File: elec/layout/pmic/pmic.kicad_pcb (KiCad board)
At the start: 2 copper layers, 14 parts, among them U1 _PCA9450AAHNY

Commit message: Fixing build errors
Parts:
- added C10, C9: 4.7µF ±10% 16V X5R, lcsc:C0603, F.Cu at (0.00, 0.00)
- added C11, C12, C13, C14, C8: 1µF ±20% 6.3V X5R, lcsc:C0201, F.Cu at (0.00, 0.00)
- added C15: 82nF ±5% 25V X7R, lcsc:C0603, F.Cu at (0.00, 0.00)
- added R1: 10kΩ ±1% 62.5mW, lcsc:R0402, F.Cu at (0.00, 0.00)
- added R2: 750mΩ ±5% 100mW, lcsc:R0603, F.Cu at (0.00, 0.00)
- C7: value 82nF ±5% 25V X7R -> 1µF ±20% 6.3V X5R; footprint lcsc:C0603 -> lcsc:C0201
- L1, L2, L3, L5, L6: value 470nH ±30% 3A - infA -> 470nH ±20% 3A - infA
- L4: value 1µH ±30% 3A - infA -> 1µH ±20% 3A - infA
- moved L1 22.6 mm to (165.1, 82.8), turned to -90 degrees
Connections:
- net *3A58.pmic-hv-0 renamed NVCC_DRAM_1V1
- net *3A58.pmic-hv-1 renamed VDD_1V8
- net *3A58.pmic-hv-2 renamed VDD_DRAM_0V9
- net *3A58.pmic-hv-3 renamed VDD_ARM_0V9
- net *3A58.pmic-hv-4 renamed VDD_SOC_0V8
- net *3A58.pmic-net-2 renamed VDD_1V8_SW
- net *3A58.pmic-net-3 renamed VDD_DRAM_0V9_SW
- net *3A58.pmic-net-4 renamed VDD_ARM_0V9_SW
- net *3A58.pmic-net-5 renamed VDD_SOC_0V8_SW
- net hv renamed VCC_3V3
- C1 pad 2: lv -> GND
- C2 pad 2: lv -> GND
- C3 pad 2: lv -> GND
- C4 pad 2: lv -> GND
- C5 pad 2: lv -> GND
- C6 pad 2: lv -> GND
- C7 pad 1: *3A58.pmic-net-6 -> NVCC_SD2
- C7 pad 2: lv -> *3A58.pmic.NVCC_SD2-lv
- L5 pad 1: *3A58.pmic-net-1 -> VDD_PHY_0V9_SW
- L6 pad 1: *3A58.pmic-net-0 -> VDDA_1V8_SW
- U1 pad 1: ldo4 -> VDD_PHY_0V9
- U1 pad 15: *3A58.pmic-net-1 -> VDD_PHY_0V9_SW
- U1 pad 16: *3A58.pmic-net-6 -> VSYS_5V
- U1 pad 17: *3A58.pmic-net-6 -> VSYS_5V
- U1 pad 18: *3A58.pmic-net-6 -> VSYS_5V
- U1 pad 2: ldo2 -> VDD_SNVS_0V8
- U1 pad 23: swout -> *3A58.pmic-net-0
- U1 pad 3: ldo1 -> NVCC_SNVS_1V8
- U1 pad 33: *3A58.pmic-net-6 -> VSYS_5V
- U1 pad 34: *3A58.pmic-net-6 -> VSYS_5V
- U1 pad 35: *3A58.pmic-net-6 -> VSYS_5V
- U1 pad 43: lv -> GND
- U1 pad 47: *3A58.pmic-net-6 -> VSYS_5V
- U1 pad 5: lv -> GND
- U1 pad 50: *3A58.pmic-net-0 -> VDDA_1V8_SW
- U1 pad 51: *3A58.pmic-net-0 -> VDDA_1V8_SW
- U1 pad 54: ldo3 -> VDDA_1V8
- U1 pad 55: ldo5 -> NVCC_SD2
- U1 pad 56: *3A58.pmic-net-6 -> VSYS_5V
- U1 pad 57: lv -> GND
- U1 pad 6: rtc_reset_b -> *3A58.pmic-net-1

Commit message: pmic layout file
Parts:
- added C16: 2.2µF ±20% 10V X5R, lcsc:C0402, B.Cu at (168.4, 88.9)
- added C17: 2.2µF ±20% 10V X5R, lcsc:C0402, B.Cu at (162.9, 88.7)
- added C18: 10µF ±10% 10V X5R, lcsc:C0603, B.Cu at (163.0, 91.2)
- added C19: 10µF ±10% 10V X5R, lcsc:C0603, B.Cu at (163.0, 90.2)
- added C20: 10µF ±10% 10V X5R, lcsc:C0603, B.Cu at (166.9, 86.3)
- added C21: 10µF ±10% 10V X5R, lcsc:C0603, B.Cu at (167.9, 86.3)
- added C22: 10µF ±10% 10V X5R, lcsc:C0603, B.Cu at (168.2, 90.8)
- added C23: 10µF ±10% 10V X5R, lcsc:C0603, B.Cu at (168.2, 89.8)
- added C24: 10µF ±10% 10V X5R, lcsc:C0603, B.Cu at (163.0, 87.9)
- added C25: 2.2µF ±20% 10V X5R, lcsc:C0402, B.Cu at (165.0, 86.4)
- added C26: 10pF ±5% 50V C0G, lcsc:C0201, F.Cu at (167.5, 93.7)
- added C27: 10pF ±5% 50V C0G, lcsc:C0201, F.Cu at (166.3, 93.7)
- added XTAL1: Crystal, lcsc:OSC-SMD_L3.2-W1.5, F.Cu at (166.9, 94.8)
- C1, C11, C12, C13, C14, C2, C3, C4, C5, C6, C7, C8, C9: moved to B.Cu
- C15: value 82nF ±5% 25V X7R -> 10µF ±10% 10V X5R; moved to B.Cu
- R1: value 10kΩ ±1% 62.5mW -> 10kΩ ±1% 50mW; footprint lcsc:R0402 -> lcsc:R0201; moved to B.Cu
- R2: value 750mΩ ±5% 100mW -> 1.5Ω ±5% 50mW; footprint lcsc:R0603 -> lcsc:R0201; moved to B.Cu
- moved C10 192.6 mm to (171.4, 87.7)
- moved R2 189.4 mm to (161.4, 99.2), turned to -90 degrees
- moved C13 189.1 mm to (161.0, 99.2), turned to -90 degrees
- moved C9 188.4 mm to (160.2, 99.2), turned to -90 degrees
- moved C14 187.6 mm to (159.2, 99.2), turned to -90 degrees
- moved R1 187.1 mm to (158.6, 99.2), turned to -90 degrees
- moved C15 187.0 mm to (165.9, 86.3), turned to -90 degrees
- moved C8 186.7 mm to (158.2, 99.2), turned to -90 degrees
- moved C12 186.4 mm to (157.8, 99.2), turned to -90 degrees
- moved C11 184.8 mm to (161.0, 90.7), turned to 180 degrees
- moved C4 33.5 mm to (172.1, 88.9), turned to 180 degrees
- moved C5 33.2 mm to (171.7, 91.3), turned to 180 degrees
- moved C3 30.1 mm to (167.5, 83.1), turned to -90 degrees
- moved L5 29.1 mm to (171.7, 91.8), turned to 180 degrees
- moved L3 27.2 mm to (167.5, 83.1), turned to -90 degrees
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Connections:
- net *3A58.pmic-lv renamed *3B78.pmic-lv
- net *3A58.pmic-net-1 renamed *3B78.pmic-net-3
- net *3A58.pmic.VDD_PHY_1V2-lv renamed *3B78.pmic.VDD_PHY_1V2-lv
- net *3A58.pmic.pmic-net renamed *3B78.pmic.pmic-net
- net signal renamed RTC_RESET_B
- C10 pad 1: *3A58.pmic-net-0 -> VCC_3V3
- C11 pad 2: *3A58.pmic.VDDA_1V8-lv -> GND
- C12 pad 2: *3A58.pmic.VDD_PHY_0V9-lv -> GND
- C14 pad 2: *3A58.pmic.VDD_SNVS_0V8-lv -> GND
- C7 pad 2: *3A58.pmic.NVCC_SD2-lv -> GND
- C8 pad 2: *3A58.pmic.NVCC_SNVS_1V8-lv -> GND
- R2 pad 2: *3A58.pmic-net-0 -> *3B78.pmic-net-2
- U1 pad 10: xtal_in -> *3B78.pmic-net-1
- U1 pad 11: xtal_out -> *3B78.pmic-net-0
- U1 pad 12: sw_en -> *3B78.pmic-net-2
- U1 pad 23: *3A58.pmic-net-0 -> VCC_3V3
- U1 pad 43: GND -> buck_agnd
- U1 pad 5: GND -> agnd
- U1 pad 57: GND -> ep
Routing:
- net *3B78.pmic-net-0: track 0.00 -> 2.88 mm
- net *3B78.pmic-net-1: track 0.00 -> 2.83 mm

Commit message: Layout 90% complete
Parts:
- added C28: 10pF ±5% 50V C0G, lcsc:C0201, F.Cu at (165.7, 93.6)
- C15: value 10µF ±10% 10V X5R -> 1µF ±20% 6.3V X5R; footprint lcsc:C0603 -> lcsc:C0201
- C16, C25: value 2.2µF ±20% 10V X5R -> 10µF ±10% 10V X5R; footprint lcsc:C0402 -> lcsc:C0603
- C18: value 10µF ±10% 10V X5R -> 2.2µF ±20% 10V X5R; footprint lcsc:C0603 -> lcsc:C0402
- C26: value 10pF ±5% 50V C0G -> 2.2µF ±20% 10V X5R; footprint lcsc:C0201 -> lcsc:C0402; moved to B.Cu
- R1: moved to F.Cu
- moved C9 15.1 mm to (172.2, 90.0), turned to 180 degrees
- moved R2 8.99 mm to (167.4, 92.5), turned to 90 degrees
- moved C8 8.85 mm to (163.8, 92.4), turned to 90 degrees
- moved C12 8.55 mm to (162.9, 92.4), turned to 90 degrees
- moved R1 8.08 mm to (164.7, 93.9)
- moved C14 8.02 mm to (163.4, 92.4), turned to 90 degrees
- moved C26 7.50 mm to (166.0, 86.3), turned to -90 degrees
- moved C15 6.22 mm to (164.3, 92.4), turned to 90 degrees
- moved C13 4.74 mm to (163.2, 95.0)
- moved C25 2.01 mm to (163.1, 86.9), turned to 0 degrees
- moved C27 1.18 mm to (167.4, 93.6), turned to 180 degrees
- moved C16 0.25 mm to (168.2, 88.7)
- moved C18 0.11 mm to (163.0, 91.1)
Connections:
- net *3B78.pmic-net-2 renamed *3AE8.pmic-net-0
- net *3B78.pmic-net-3 renamed *3AE8.pmic-net-2
- net *3B78.pmic.VDD_PHY_1V2-lv renamed lv
- net *3B78.pmic.pmic-net renamed *3AE8.pmic.pmic-net
- net VDD_1V8_SW renamed VDD_3V3_SW
- C10 pad 2: *3B78.pmic-lv -> GND
- C15 pad 1: VSYS_5V -> *3AE8.pmic-net-4
- C26 pad 1: *3B78.pmic-net-0 -> VSYS_5V
- C27 pad 1: *3B78.pmic-net-1 -> *3AE8.pmic-net-1
- U1 pad 10: *3B78.pmic-net-1 -> *3AE8.pmic-net-3
- U1 pad 11: *3B78.pmic-net-0 -> *3AE8.pmic-net-1
- U1 pad 14: buck5fb -> VDD_1V8
- U1 pad 21: VDD_1V8 -> VCC_3V3
- U1 pad 4: vint -> *3AE8.pmic-net-4
- U1 pad 43: buck_agnd -> GND
- U1 pad 5: agnd -> GND
- U1 pad 53: vsys -> VSYS_5V
- U1 pad 57: ep -> GND
- XTAL1 pad 1: *3B78.pmic-net-0 -> *3AE8.pmic-net-1
- XTAL1 pad 2: *3B78.pmic-net-1 -> *3AE8.pmic-net-3
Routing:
- net GND: track 0.00 -> 8.49 mm, vias 0 -> 20
- net *3B78.pmic-net-0: track 2.88 -> 0.00 mm
- net *3AE8.pmic-net-0: track 0.00 -> 2.88 mm
- net *3B78.pmic-net-1: track 2.83 -> 0.00 mm
- net *3AE8.pmic-net-2: track 0.00 -> 2.83 mm
- net *3AE8.pmic-net-4: track 0.00 -> 1.37 mm
- net VCC_3V3: track 0.00 -> 1.30 mm, vias 0 -> 3
- net NVCC_SNVS_1V8: track 0.00 -> 1.10 mm, vias 0 -> 1
- net VDD_SNVS_0V8: track 0.00 -> 1.10 mm, vias 0 -> 1
- net *3AE8.pmic-net-1: track 0.00 -> 1.10 mm, vias 0 -> 1
- net *3AE8.pmic-net-3: track 0.00 -> 1.08 mm, vias 0 -> 1
- net VDD_PHY_0V9: track 0.00 -> 1.07 mm, vias 0 -> 1
- net VDDA_1V8: track 0.00 -> 0.86 mm, vias 0 -> 1
- net NVCC_SD2: track 0.00 -> 0.85 mm, vias 0 -> 1
- net VDD_1V8: track 0.00 -> 0.45 mm, vias 0 -> 1
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- added copper zone on F.Cu, net VCC_3V3
- added copper zone on F.Cu, net VDDA_1V8_SW
- added copper zone on F.Cu, net VDD_3V3_SW
- added copper zone on F.Cu, net VDD_ARM_0V9_SW
- added copper zone on F.Cu, net VDD_PHY_0V9_SW
- added copper zone on F.Cu, net VDD_SOC_0V8_SW
- added copper zone on F.Cu, net VSYS_5V

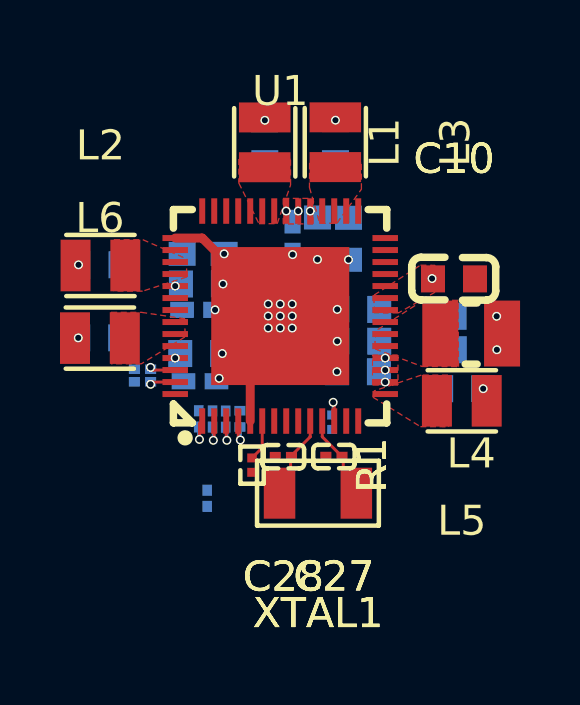
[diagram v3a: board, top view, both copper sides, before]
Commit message: add extra LDO for 1v2 rail
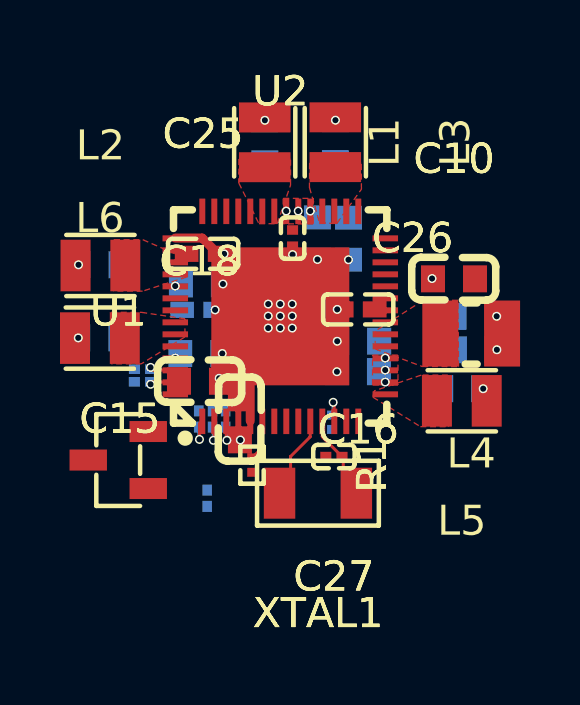
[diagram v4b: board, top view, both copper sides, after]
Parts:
- removed C28: 10pF ±5% 50V C0G, lcsc:C0201
- added U2: _PCA9450AAHNY, lcsc:HVQFN-56_L7.0-W7.0-P0.40-BL-EP4.6, F.Cu at (165.6, 88.9)
- C15: value 1µF ±20% 6.3V X5R -> 10µF ±10% 10V X5R; footprint lcsc:C0201 -> lcsc:C0603; moved to F.Cu
- C16, C25: value 10µF ±10% 10V X5R -> 2.2µF ±20% 10V X5R; footprint lcsc:C0603 -> lcsc:C0402; moved to F.Cu
- C18: value 2.2µF ±20% 10V X5R -> 10µF ±10% 10V X5R; footprint lcsc:C0402 -> lcsc:C0603; moved to F.Cu
- C26: value 2.2µF ±20% 10V X5R -> 10pF ±5% 50V C0G; footprint lcsc:C0402 -> lcsc:C0201; moved to F.Cu
- U1: value _PCA9450AAHNY -> LDO 1.2V Vin max 3.3V - infV Iq; footprint lcsc:HVQFN-56_L7.0-W7.0-P0.40-BL-EP4.6 -> lcsc:SOT-23-3_L2.9-W1.3-P1.90-LS2.4-BR
- moved U1 7.22 mm to (160.2, 93.7)
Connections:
- C13 pad 2: lv -> GND
- C15 pad 1: *3AE8.pmic-net-4 -> VSYS_5V
- C26 pad 1: VSYS_5V -> *3A58.pmic-net-0
- C27 pad 1: *3AE8.pmic-net-1 -> *3A58.pmic-net-1
- R1 pad 1: *3AE8.pmic-net-2 -> *3A58.pmic-net-3
- R2 pad 2: *3AE8.pmic-net-0 -> *3A58.pmic-net-2
- U1 pad 1: VDD_PHY_0V9 -> GND
- U1 pad 2: VDD_SNVS_0V8 -> VDD_PHY_1V2
- U1 pad 3: NVCC_SNVS_1V8 -> VCC_3V3
- XTAL1 pad 1: *3AE8.pmic-net-1 -> *3A58.pmic-net-0
- XTAL1 pad 2: *3AE8.pmic-net-3 -> *3A58.pmic-net-1
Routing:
- net (no net): track 0.00 -> 3.98 mm, vias 0 -> 1
- net *3AE8.pmic-net-0: track 2.88 -> 0.00 mm
- net *3AE8.pmic-net-2: track 2.83 -> 0.00 mm
- net *3A58.pmic-net-1: track 0.00 -> 2.83 mm
- net *3AE8.pmic-net-4: track 1.37 -> 0.00 mm
- net *3A58.pmic-net-3: track 0.00 -> 1.37 mm
- net *3AE8.pmic-net-1: track 1.10 -> 0.00 mm, vias 1 -> 0
- net *3AE8.pmic-net-3: track 1.08 -> 0.00 mm, vias 1 -> 0
- net *3A58.pmic-net-2: track 0.00 -> 1.08 mm, vias 0 -> 1
- removed copper zone on F.Cu, net VCC_3V3

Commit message: Update ato.yaml to build nonos + import into layout
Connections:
- net *3A58.pmic-net-0 renamed *E8E8-net-0
- net *3A58.pmic-net-1 renamed *E8E8-net-1
- net *3A58.pmic-net-2 renamed *E8E8-net-3
- net *3A58.pmic-net-3 renamed *E8E8-net-2
- net *3A58.pmic.pmic-net renamed *E8E8.pmic-net

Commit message: update naming
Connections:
- net *E8E8-net-0 renamed *F6F8-net-1
- net *E8E8-net-1 renamed *F6F8-net-2
- net *E8E8-net-2 renamed *F6F8-net-3
- net *E8E8-net-3 renamed *F6F8-net-0
- net *E8E8.pmic-net renamed *F6F8.pmic-net
